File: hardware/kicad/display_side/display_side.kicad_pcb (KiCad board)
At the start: 2 copper layers, 85 x 65 mm, 34 parts, among them J1 RJ45, J2 EPD_FFC_24, J3 UART-DBG, J4 USB-OTG, U1 R-78E3.3-0.5, U2 SN65HVD3082E

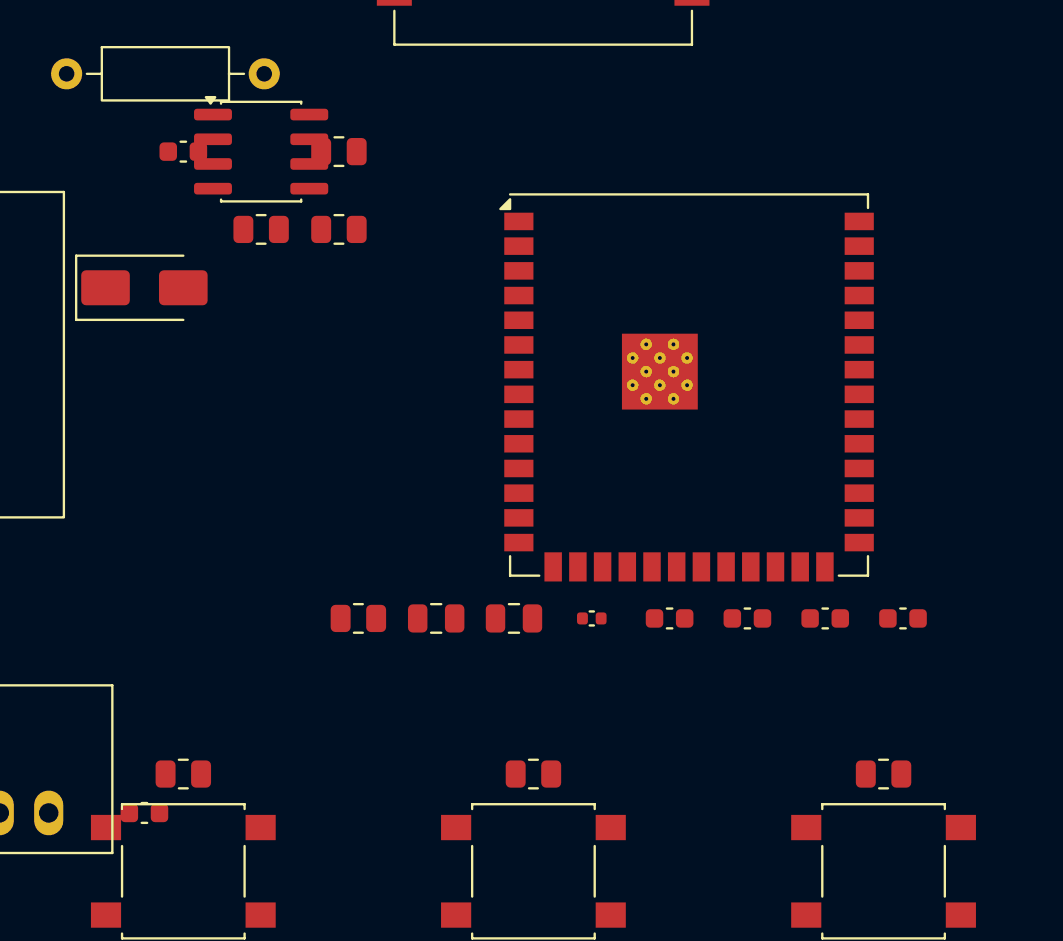
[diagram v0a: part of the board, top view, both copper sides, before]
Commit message: hardware: CP4 iter-4 — net-correctness audit + solder-mask cleanup
Addresses iter-3 Findings 04-05.

Finding 04 (BLOCKER — DISAGREE): The 10 D11 iter-2 evidence PNGs
ARE committed on origin/hw/cp4-display-placement at the paths the
packet references; verified via git ls-tree from commit 8f55759.
Counter-evidence pasted in §9.4 RESOLVED entry. iter-4 also adds
MANIFEST.sha256 under iter4/ for deterministic reviewer
verification going forward (mirrors cp_schematic_cleanup pattern).

Finding 05 (IMPORTANT — AGREE + extra). Two distinct root causes:

(a) Net-correctness audit. Investigating the BTN1_IN/BTN3_IN
solder_mask_bridge between BTN1 pad 1 and C10 pad 1 revealed
iter-2 misidentified C5/C8/C9/C10. Per display_side.net:
  C5  = ESP_EN debounce (ESP_EN ↔ GND), not "1µF V3V3 bulk"
  C8  = BTN1_IN debounce, not "MOD1 IO bypass"
  C9  = BTN2_IN debounce, not "MOD1 IO bypass"
  C10 = BTN3_IN debounce, not "U1 V3V3-out bypass"
Iter-4 moves: C8→(26,50) with R5 above BTN1; C9→(44,50) with R6
above BTN2; C10→(62,50) with R7 above BTN3; C5→(33,39.5) next to
R1 EN-pullup near MOD1 EN pin. C2/C3/C4/C6/C7 remain on the V3V3
decoupling row (those are the actual MOD1 bypass caps).

(b) U2 pad-spacing cleanup. R3/R4 (RS-485 fail-safe bias) moved
from X=32 to X=34 (6mm right of U2 anchor, was 4mm). U2 pads 6/7
sit at X≈30.4; R3 pad 1 at X=31.09 was inside the mask web. New
position gives clean unlike-net mask aperture.

DRC results: 0 solder_mask_bridge (was 5), 0 hole_clearance errors
(was 1), 93 total violations (was 112). Remaining 93 are
footprint-internal silk/drill noise and intentional B.Cu under-IC
adjacency, matching battery-side baseline character.

Per-region D11 inspection at iter4/ shows BTN row and U2 cluster
both improved (R+C pair per button visible, R3/R4 clear of U2
pads). Carry-over from iter-2: BTN1/2/3 designator silk hidden
under button bodies (tracked for iter-5+).

SEMAPHORE flipped to codex_turn at iteration 5.

Co-Authored-By: Claude Opus 4.7 (1M context)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
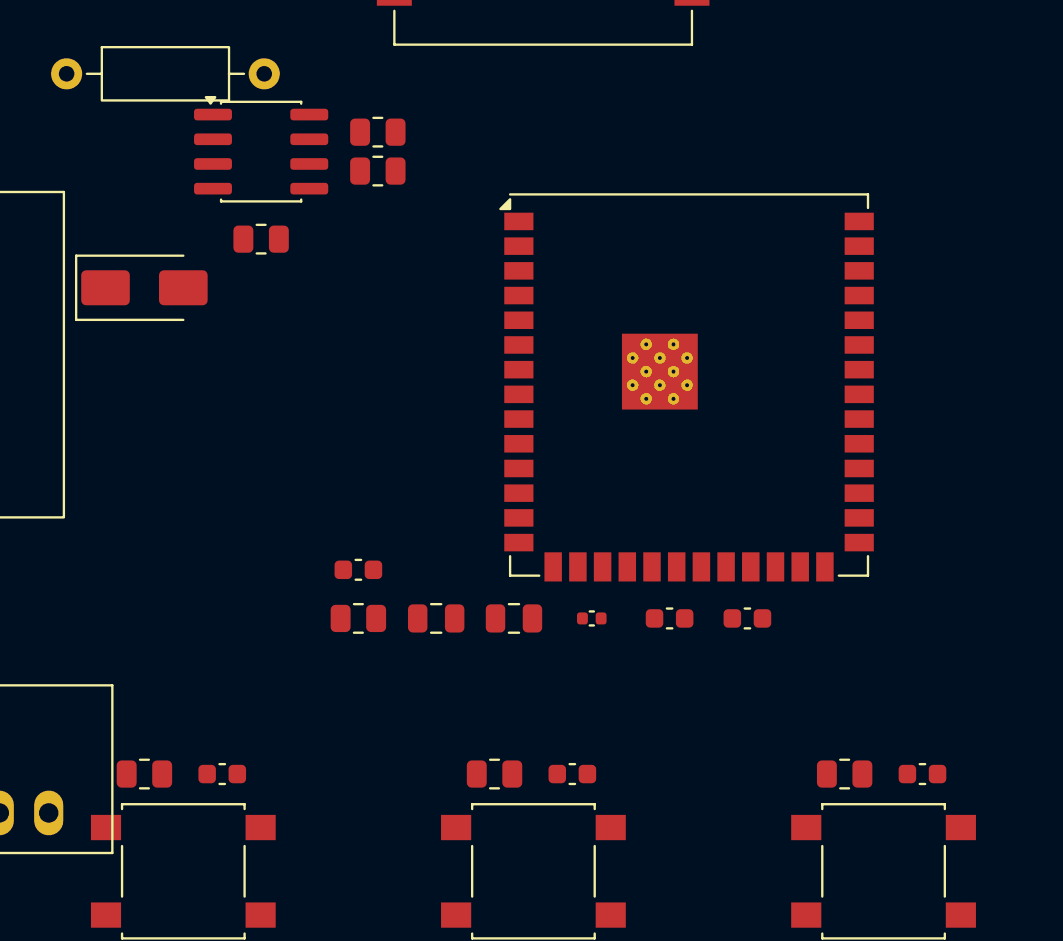
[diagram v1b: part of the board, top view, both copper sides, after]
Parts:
- moved C10 40.0 mm to (62.0, 50.0)
- moved C7 37.6 mm to (53.0, 42.0)
- moved C8 32.0 mm to (26.0, 50.0)
- moved C9 18.8 mm to (44.0, 50.0)
- moved C5 16.2 mm to (33.0, 39.5)
- moved C6 4.00 mm to (49.0, 42.0)
- moved R4 3.61 mm to (34.0, 19.0)
- moved R3 2.24 mm to (34.0, 17.0)
- moved R5 2.00 mm to (22.0, 50.0)
- moved R6 2.00 mm to (40.0, 50.0)
- moved R7 2.00 mm to (58.0, 50.0)
- moved R2 0.50 mm to (28.0, 22.5)
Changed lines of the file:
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@@
   )
   (footprint "volthium:C_0603_1608Metric" (version 20260206) (generator kicad-footprint-generator) (layer "B.Cu")
-    (at 22.0 52.0 0)
+    (at 62.0 50.0 0)
     (descr "Capacitor SMD 0603 (1608 Metric), square (rectangular) end terminal, IPC-7351 nominal, (Body size source: IPC-SM-782 page 76, https://www.pcb-3d.com/wordpress/wp-content/uploads/ipc-sm-782a_amendment_1_and_2.pdf)")
     (tags "capacitor")
@@
   )
   (footprint "volthium:C_0603_1608Metric" (version 20260206) (generator kicad-footprint-generator) (layer "B.Cu")
-    (at 49.0 42.0 0)
+    (at 33.0 39.5 0)
     (descr "Capacitor SMD 0603 (1608 Metric), square (rectangular) end terminal, IPC-7351 nominal, (Body size source: IPC-SM-782 page 76, https://www.pcb-3d.com/wordpress/wp-content/uploads/ipc-sm-782a_amendment_1_and_2.pdf)")
     (tags "capacitor")
@@
   )
   (footprint "volthium:C_0603_1608Metric" (version 20260206) (generator kicad-footprint-generator) (layer "B.Cu")
-    (at 53.0 42.0 0)
+    (at 49.0 42.0 0)
     (descr "Capacitor SMD 0603 (1608 Metric), square (rectangular) end terminal, IPC-7351 nominal, (Body size source: IPC-SM-782 page 76, https://www.pcb-3d.com/wordpress/wp-content/uploads/ipc-sm-782a_amendment_1_and_2.pdf)")
     (tags "capacitor")
@@
   )
   (footprint "volthium:C_0603_1608Metric" (version 20260206) (generator kicad-footprint-generator) (layer "B.Cu")
-    (at 24.0 18.0 0)
+    (at 53.0 42.0 0)
     (descr "Capacitor SMD 0603 (1608 Metric), square (rectangular) end terminal, IPC-7351 nominal, (Body size source: IPC-SM-782 page 76, https://www.pcb-3d.com/wordpress/wp-content/uploads/ipc-sm-782a_amendment_1_and_2.pdf)")
     (tags "capacitor")
@@
   )
   (footprint "volthium:C_0603_1608Metric" (version 20260206) (generator kicad-footprint-generator) (layer "B.Cu")
-    (at 57.0 42.0 0)
+    (at 26.0 50.0 0)
     (descr "Capacitor SMD 0603 (1608 Metric), square (rectangular) end terminal, IPC-7351 nominal, (Body size source: IPC-SM-782 page 76, https://www.pcb-3d.com/wordpress/wp-content/uploads/ipc-sm-782a_amendment_1_and_2.pdf)")
     (tags "capacitor")
@@
   )
   (footprint "volthium:C_0603_1608Metric" (version 20260206) (generator kicad-footprint-generator) (layer "B.Cu")
-    (at 61.0 42.0 0)
+    (at 44.0 50.0 0)
     (descr "Capacitor SMD 0603 (1608 Metric), square (rectangular) end terminal, IPC-7351 nominal, (Body size source: IPC-SM-782 page 76, https://www.pcb-3d.com/wordpress/wp-content/uploads/ipc-sm-782a_amendment_1_and_2.pdf)")
     (tags "capacitor")
@@
   )
   (footprint "volthium:R_0805_2012Metric" (version 20260206) (generator kicad-footprint-generator) (layer "B.Cu")
-    (at 28.0 22.0 0)
+    (at 28.0 22.5 0)
     (descr "Resistor SMD 0805 (2012 Metric), square (rectangular) end terminal, IPC-7351 nominal, (Body size source: IPC-SM-782 page 72, https://www.pcb-3d.com/wordpress/wp-content/uploads/ipc-sm-782a_amendment_1_and_2.pdf)")
     (tags "resistor")
@@
   )
   (footprint "volthium:R_0805_2012Metric" (version 20260206) (generator kicad-footprint-generator) (layer "B.Cu")
-    (at 32.0 18.0 0)
+    (at 34.0 17.0 0)
     (descr "Resistor SMD 0805 (2012 Metric), square (rectangular) end terminal, IPC-7351 nominal, (Body size source: IPC-SM-782 page 72, https://www.pcb-3d.com/wordpress/wp-content/uploads/ipc-sm-782a_amendment_1_and_2.pdf)")
     (tags "resistor")
@@
   )
   (footprint "volthium:R_0805_2012Metric" (version 20260206) (generator kicad-footprint-generator) (layer "B.Cu")
-    (at 32.0 22.0 0)
+    (at 34.0 19.0 0)
     (descr "Resistor SMD 0805 (2012 Metric), square (rectangular) end terminal, IPC-7351 nominal, (Body size source: IPC-SM-782 page 72, https://www.pcb-3d.com/wordpress/wp-content/uploads/ipc-sm-782a_amendment_1_and_2.pdf)")
     (tags "resistor")
@@
   )
   (footprint "volthium:R_0805_2012Metric" (version 20260206) (generator kicad-footprint-generator) (layer "B.Cu")
-    (at 24.0 50.0 0)
+    (at 22.0 50.0 0)
     (descr "Resistor SMD 0805 (2012 Metric), square (rectangular) end terminal, IPC-7351 nominal, (Body size source: IPC-SM-782 page 72, https://www.pcb-3d.com/wordpress/wp-content/uploads/ipc-sm-782a_amendment_1_and_2.pdf)")
     (tags "resistor")
@@
   )
   (footprint "volthium:R_0805_2012Metric" (version 20260206) (generator kicad-footprint-generator) (layer "B.Cu")
-    (at 42.0 50.0 0)
+    (at 40.0 50.0 0)
     (descr "Resistor SMD 0805 (2012 Metric), square (rectangular) end terminal, IPC-7351 nominal, (Body size source: IPC-SM-782 page 72, https://www.pcb-3d.com/wordpress/wp-content/uploads/ipc-sm-782a_amendment_1_and_2.pdf)")
     (tags "resistor")
@@
   )
   (footprint "volthium:R_0805_2012Metric" (version 20260206) (generator kicad-footprint-generator) (layer "B.Cu")
-    (at 60.0 50.0 0)
+    (at 58.0 50.0 0)
     (descr "Resistor SMD 0805 (2012 Metric), square (rectangular) end terminal, IPC-7351 nominal, (Body size source: IPC-SM-782 page 72, https://www.pcb-3d.com/wordpress/wp-content/uploads/ipc-sm-782a_amendment_1_and_2.pdf)")
     (tags "resistor")
